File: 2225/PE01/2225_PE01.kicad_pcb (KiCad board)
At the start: 2 copper layers, 200 x 60 mm, 95 parts

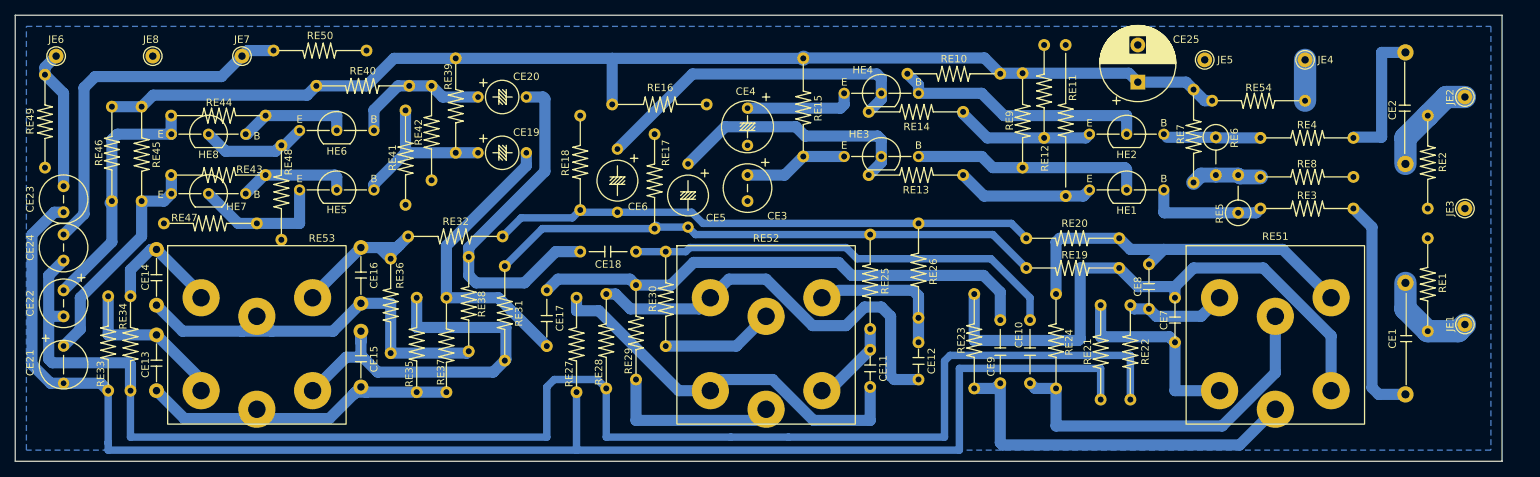
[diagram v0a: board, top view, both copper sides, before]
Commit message: Changed footprints of RE5 and RE6 from vertical resistors to horizontal
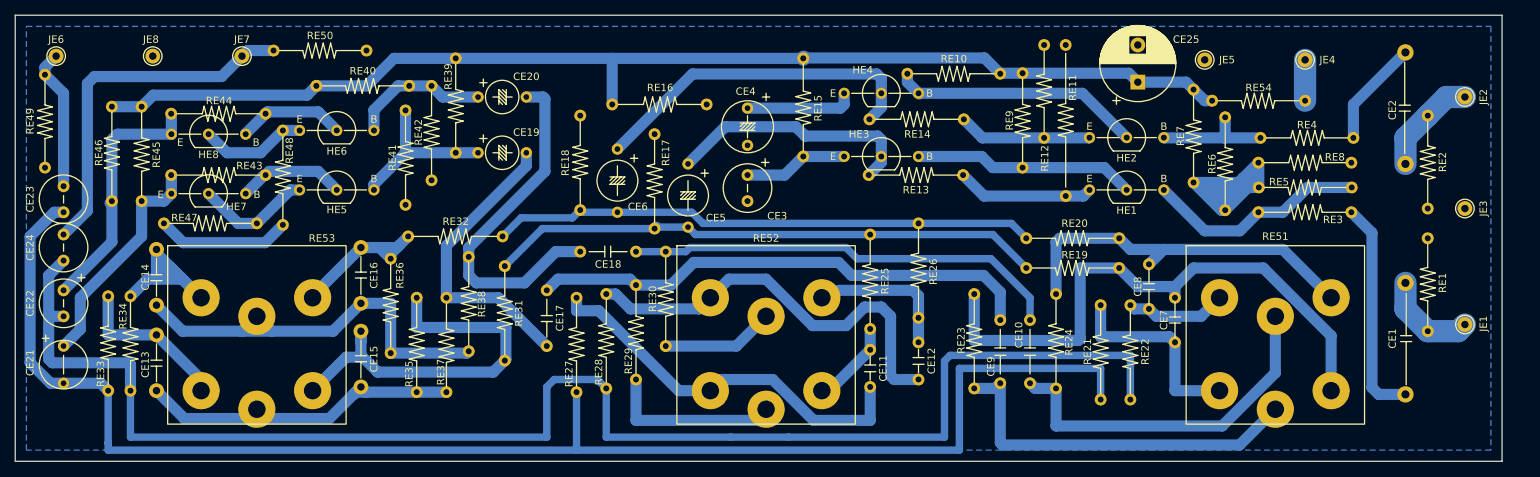
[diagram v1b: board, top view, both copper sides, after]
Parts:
- RE5, RE6: footprint Resistor_THT:R_Axial_DIN0309_L9.0mm_D3.2mm_P5.08mm_Vertical_Flipped -> Resistor_THT:R_US_Axial_DIN0309_L9.0mm_D3.2mm_P12.50mm_Horizontal
- moved RE6 4.89 mm to (162.8, 26.2)
- moved RE5 3.24 mm to (167.3, 23.2), turned to 0 degrees
- moved RE48 2.01 mm to (36.0, 15.5)
- moved RE8 1.94 mm to (179.7, 19.8)
- moved RE14 1.00 mm to (127.6, 14.0)
- moved RE3 0.57 mm to (179.7, 26.5)
- moved HE2 0.46 mm to (144.5, 16.5)
- moved RE44 0.25 mm to (33.7, 13.2)
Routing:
- net Net-(RE5-Pad1): track 9.52 -> 45.4 mm
- net Net-(CE25-Pad2): track 0.00 -> 18.1 mm
- net Net-(RE53-Pad6): track 17.2 -> 31.6 mm
- net Net-(HE1-Pad3): track 16.3 -> 30.0 mm
- net Net-(CE2-Pad2): track 18.5 -> 14.4 mm
- net Net-(HE5-Pad1): track 18.4 -> 15.8 mm
- net Net-(HE2-Pad3): track 13.2 -> 15.8 mm
- net Net-(HE1-Pad2): track 31.5 -> 29.9 mm
- net Net-(HE2-Pad2): track 35.0 -> 33.9 mm
- net Net-(CE6-Pad1): track 45.1 -> 46.1 mm
- net Net-(HE2-Pad1): track 18.8 -> 18.0 mm
- net Net-(HE6-Pad2): track 15.3 -> 14.6 mm
- net Net-(HE5-Pad2): track 15.1 -> 14.5 mm

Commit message: Changed transistor footprints to common packaging spec. Also fixed some trace intersections.
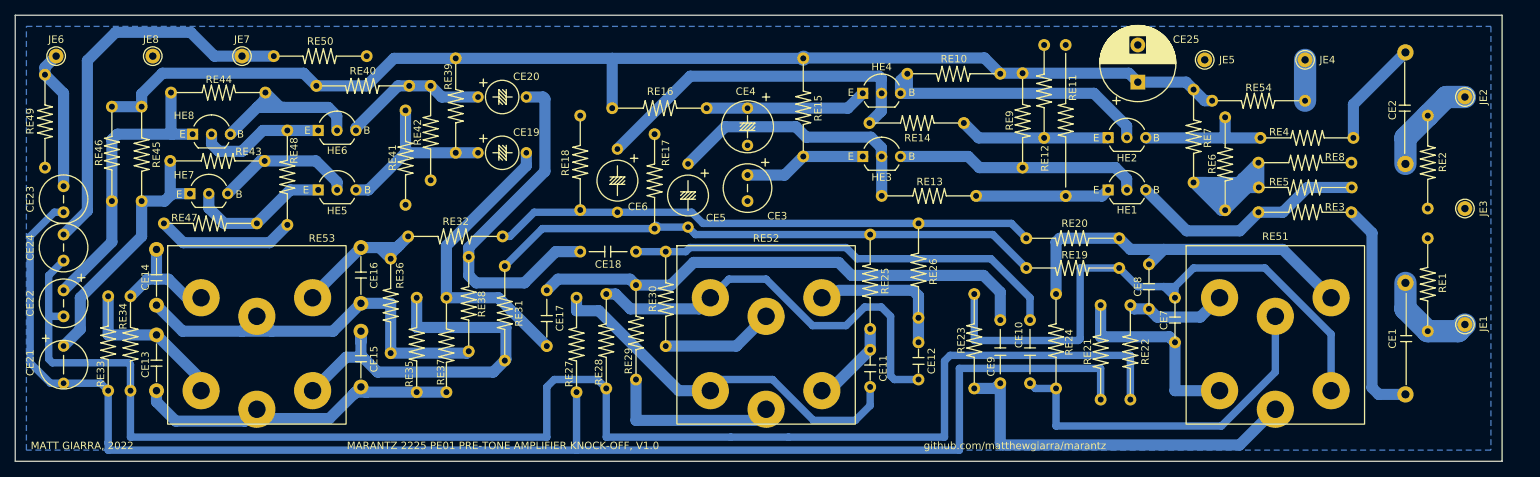
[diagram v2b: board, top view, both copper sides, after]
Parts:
- HE1, HE2, HE3, HE4, HE5, HE6, HE7, HE8: footprint Package_TO_SOT_THT:TO-92_Inline_Wide_10mm -> Package_TO_SOT_THT:TO-92_Inline_Wide
- moved RE13 3.30 mm to (129.2, 24.3)
- moved HE8 2.86 mm to (23.9, 16.0)
- moved RE44 2.85 mm to (33.6, 10.4)
- moved HE1 2.50 mm to (147.0, 23.5)
- moved HE2 2.50 mm to (147.0, 16.5)
- moved HE3 2.50 mm to (114.0, 19.0)
- moved HE4 2.50 mm to (114.0, 10.5)
- moved HE5 2.50 mm to (40.8, 23.5)
- moved HE6 2.50 mm to (40.8, 15.5)
- moved HE7 2.50 mm to (23.5, 24.0)
- moved RE43 1.90 mm to (33.5, 19.6)
- moved RE50 0.75 mm to (34.8, 5.50)
- moved RE48 0.60 mm to (36.6, 15.5)
- moved RE14 0.50 mm to (127.6, 14.5)
- moved RE16 0.50 mm to (93.0, 12.5)
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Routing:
- net Net-(RE53-Pad6): track 31.6 -> 16.5 mm
- net Net-(HE6-Pad2): track 14.6 -> 26.1 mm
- net Net-(CE4-Pad1): track 14.7 -> 21.8 mm
- net Net-(HE2-Pad2): track 33.9 -> 39.5 mm
- net Net-(CE22-Pad1): track 34.4 -> 39.8 mm
- net Net-(HE5-Pad2): track 14.5 -> 18.8 mm
- net Net-(CE21-Pad1): track 30.8 -> 35.0 mm
- net Net-(CE24-Pad2): track 48.5 -> 52.7 mm
- net Net-(HE5-Pad1): track 15.8 -> 19.4 mm
- net Net-(HE1-Pad2): track 29.9 -> 33.2 mm
- net Net-(CE25-Pad1): track 159.3 -> 162.2 mm
- net Net-(HE6-Pad1): track 14.5 -> 17.2 mm
- net Net-(CE3-Pad1): track 14.0 -> 16.5 mm
- net Net-(HE1-Pad3): track 30.0 -> 32.4 mm
- net Net-(HE2-Pad3): track 15.8 -> 18.2 mm
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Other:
- board text added: "MARANTZ 2225 PE01 PRE-TONE AMPLIFIER KNOCK-OFF, V1.0"
- board text added: "MATT GIARRA, 2022"
- board text added: "github.com/matthewgiarra/marantz"

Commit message: Changed some capacitor footprints to match real components
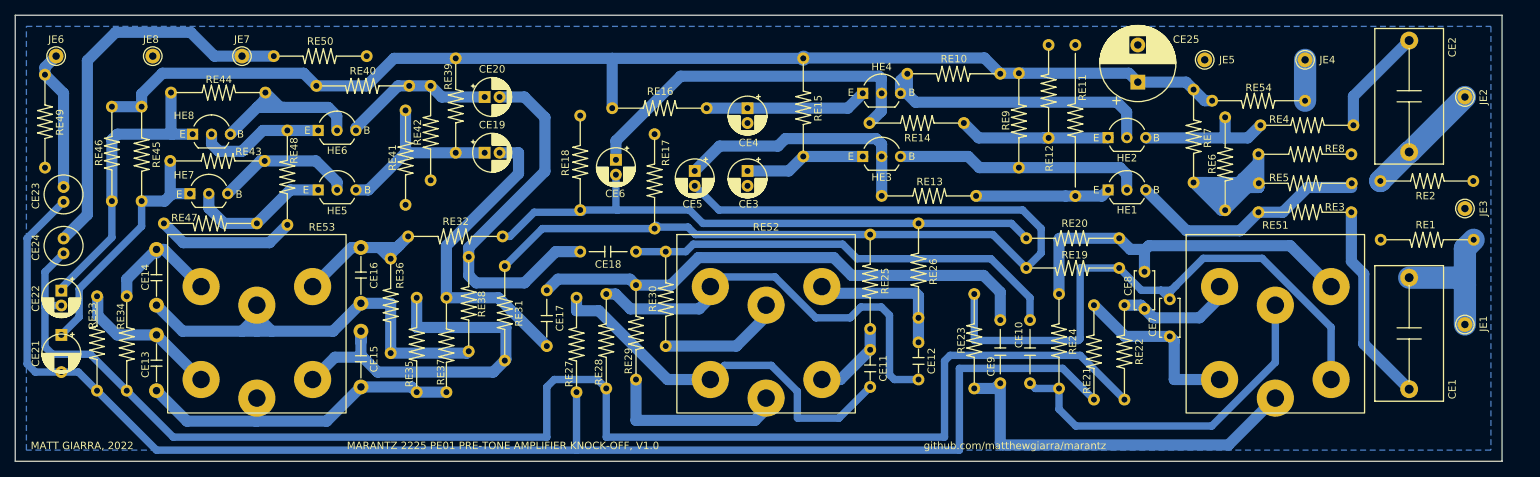
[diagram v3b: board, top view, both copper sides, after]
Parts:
- CE1, CE2: footprint Capacitor_THT:C_US_Rect_L16.5mm_W4.7mm_P15.00mm_MKT -> Capacitor_THT:C_US_Rect_L18.0mm_W9.0mm_P15.00mm_FKS3_FKP3
- CE19, CE20: footprint Capacitor_THT:CP_Electrolytic_Radial_D4.5mm_P6.50mm -> Capacitor_THT:CP_Radial_D5.0mm_P2.00mm
- CE21: footprint Capacitor_THT:CP_Radial_D6.3mm_P5.0mm -> Capacitor_THT:CP_Radial_D5.0mm_P5.00mm
- CE22, CE3: footprint Capacitor_THT:CP_Radial_D6.3mm_H11.0mm_P3.50mm -> Capacitor_THT:CP_Radial_D5.0mm_P2.00mm
- CE23, CE24: footprint Capacitor_THT:C_Radial_D6.3mm_H11.0mm_P3.50mm -> Capacitor_THT:C_Radial_D5.0mm_H11.0mm_P2.00mm
- CE4: footprint Capacitor_THT:CP_Radial_D7.0mm_P5.00mm -> Capacitor_THT:CP_Radial_D5.0mm_P2.00mm
- CE5, CE6: footprint Capacitor_THT:CP_Electrolytic_Radial_D5.5mm_P8.50mm -> Capacitor_THT:CP_Radial_D5.0mm_P2.00mm
- CE7, CE8: footprint Capacitor_THT:C_US_Disc_D7.0mm_W2.5mm_P6.00mm -> Capacitor_THT:C_Disc_D5.0mm_W2.5mm_P5.00mm
- moved RE2 7.16 mm to (196.1, 22.3), turned to 180 degrees
- moved RE1 6.33 mm to (183.7, 30.2), turned to 0 degrees
- moved RE4 1.70 mm to (180.0, 14.8)
- moved CE2 1.68 mm to (187.5, 18.4)
- moved RE33 1.50 mm to (11.0, 37.8)
- moved RE51 1.50 mm to (162.0, 49.0)
- moved RE52 1.50 mm to (93.5, 49.0)
- moved RE53 1.50 mm to (25.0, 49.0)
- moved CE6 1.46 mm to (80.8, 19.4)
- moved CE23 1.40 mm to (6.50, 25.1)
- moved CE5 1.30 mm to (91.4, 20.9)
- moved RE11 1.30 mm to (142.6, 4.00)
- moved RE8 1.13 mm to (179.7, 18.7)
- moved CE7 1.06 mm to (155.3, 43.2)
- moved CE24 0.97 mm to (6.50, 32.0)
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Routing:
- net Net-(CE5-Pad2): track 74.6 -> 129.7 mm
- net Net-(CE22-Pad2): track 202.4 -> 193.3 mm
- net Net-(CE21-Pad2): track 199.5 -> 192.7 mm
- net Net-(CE1-Pad1): track 13.4 -> 20.1 mm
- net Net-(CE6-Pad2): track 73.6 -> 78.9 mm
- net Net-(RE53-Pad5): track 57.5 -> 62.5 mm
- net Net-(RE51-Pad1): track 27.1 -> 24.1 mm
- net Net-(CE1-Pad2): track 29.6 -> 27.0 mm
- net Net-(RE52-Pad4): track 17.3 -> 19.8 mm
- net Net-(RE51-Pad6): track 13.7 -> 16.1 mm
- net Net-(CE2-Pad1): track 13.8 -> 16.1 mm
- net Net-(CE6-Pad1): track 46.3 -> 48.6 mm
- net Net-(RE5-Pad1): track 45.4 -> 47.6 mm
- net Net-(CE18-Pad2): track 47.8 -> 49.9 mm
- net Net-(CE17-Pad2): track 40.1 -> 42.3 mm
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
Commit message: Updated footprints of CE9 - CE12. Changed some trace widths to 0.5mm
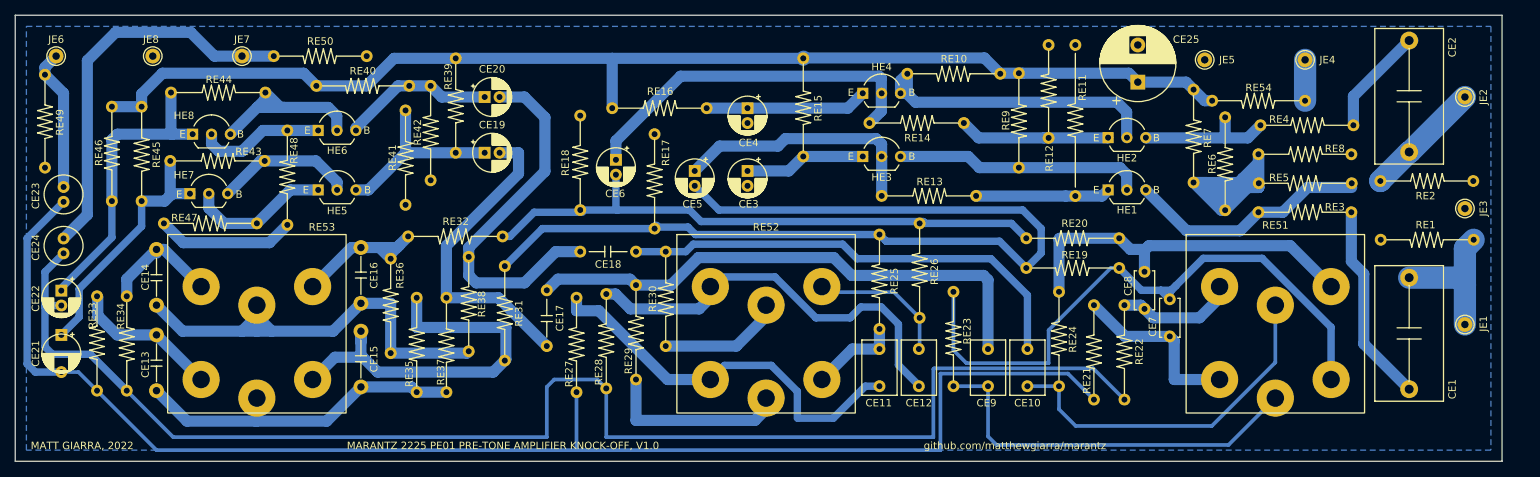
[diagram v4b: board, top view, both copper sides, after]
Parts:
- CE10, CE9: footprint Capacitor_THT:C_Rect_L7.2mm_W3.5mm_P8.50mm -> Capacitor_THT:C_Rect_L7.2mm_W4.5mm_P5.00mm_FKS2_FKP2_MKS2_MKP2
- CE11, CE12: footprint Capacitor_THT:C_US_Rect_L7.2mm_W3.5mm_P5.00mm_FKS2_FKP2_MKS2_MKP2 -> Capacitor_THT:C_Rect_L7.2mm_W4.5mm_P5.00mm_FKS2_FKP2_MKS2_MKP2
- moved RE23 2.82 mm to (126.2, 37.2)
- moved CE9 1.70 mm to (130.8, 49.9)
- moved CE11 1.25 mm to (116.2, 49.9)
- moved RE25 1.25 mm to (116.2, 29.5)
- moved CE12 0.90 mm to (121.5, 49.9)
- moved CE10 0.53 mm to (136.2, 49.9)
- moved RE24 0.30 mm to (140.4, 37.2)
- moved RE26 0.15 mm to (121.7, 28.0)
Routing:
- net Net-(CE10-Pad2): track 59.4 -> 62.9 mm
- net Net-(RE51-Pad3): track 81.6 -> 85.1 mm
- net Net-(CE17-Pad1): track 69.2 -> 72.2 mm
- net Net-(CE22-Pad2): track 193.3 -> 191.2 mm
- net Net-(RE51-Pad2): track 51.6 -> 53.5 mm
- net Net-(RE52-Pad1): track 52.6 -> 53.8 mm
- net Net-(RE52-Pad3): track 11.0 -> 12.1 mm
- net Net-(CE21-Pad2): track 192.7 -> 191.7 mm
- net Net-(RE52-Pad6): track 55.6 -> 54.7 mm
- net Net-(RE52-Pad4): track 19.8 -> 20.4 mm

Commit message: Changed footprint of CE13 and CE14 to real WIMA caps.
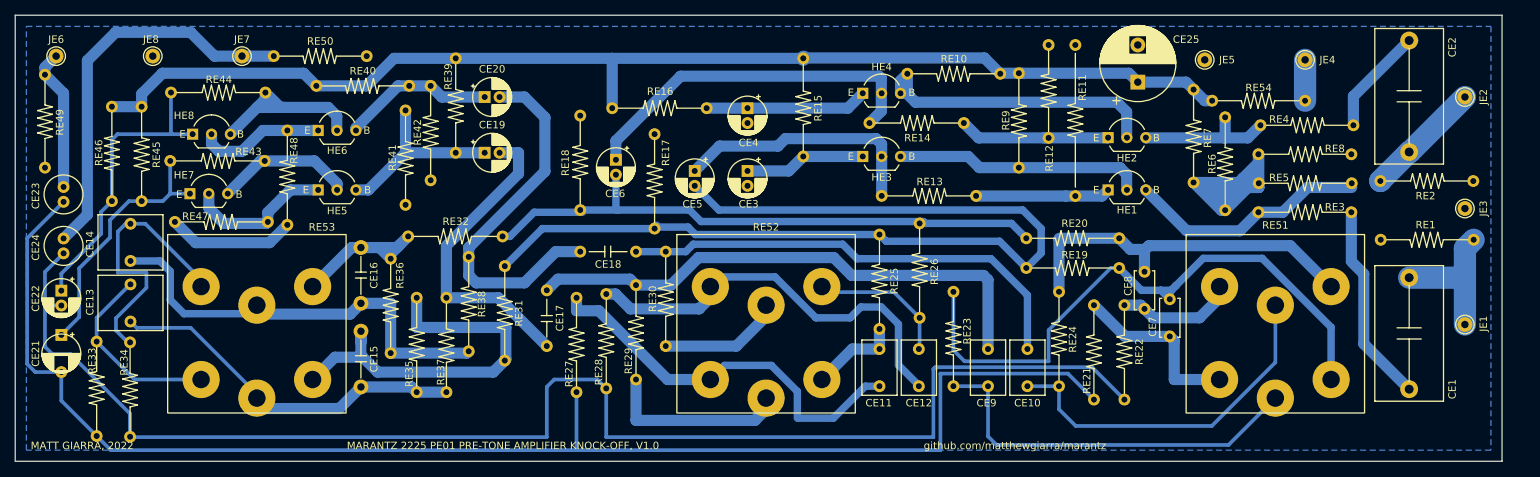
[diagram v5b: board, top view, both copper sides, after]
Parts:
- CE13, CE14: footprint Capacitor_THT:C_US_Rect_L10.0mm_W4.0mm_P7.50mm_FKS3_FKP3 -> Capacitor_THT:C_Rect_L7.2mm_W8.5mm_P5.00mm_FKP2_FKP2_MKS2_MKP2
- moved CE13 7.65 mm to (15.5, 36.2)
- moved RE34 6.22 mm to (15.4, 56.7)
- moved RE33 6.10 mm to (10.9, 43.9)
- moved CE14 4.91 mm to (15.5, 28.1)
- moved RE47 1.49 mm to (21.5, 27.8)
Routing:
- net Net-(RE53-Pad6): track 17.0 -> 37.7 mm
- net Net-(CE22-Pad2): track 191.2 -> 196.7 mm
- net Net-(RE53-Pad1): track 21.6 -> 26.7 mm
- net Net-(RE53-Pad2): track 46.0 -> 49.4 mm
- net Net-(CE21-Pad2): track 191.7 -> 194.1 mm
- net Net-(RE53-Pad5): track 62.5 -> 60.7 mm
- net Net-(CE25-Pad2): track 18.7 -> 17.3 mm
- net Net-(CE21-Pad1): track 33.6 -> 34.4 mm
- net Net-(HE5-Pad1): track 19.4 -> 20.1 mm

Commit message: Updated capacitor footprints to represent available components
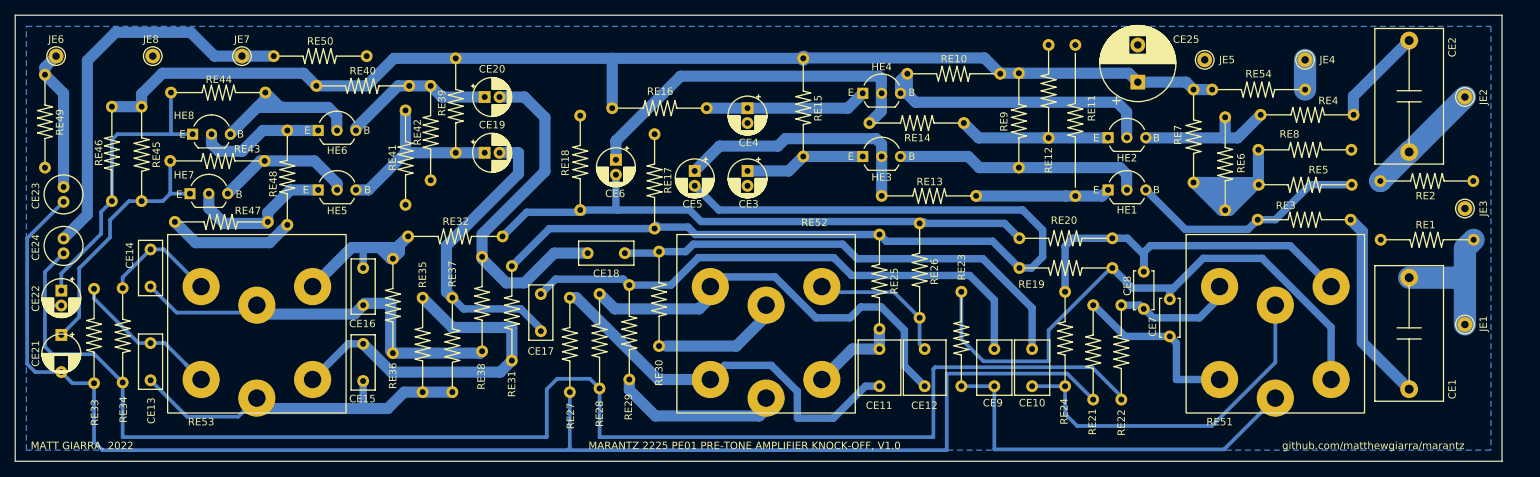
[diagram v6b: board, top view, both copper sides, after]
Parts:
- CE11, CE12: footprint Capacitor_THT:C_Rect_L7.2mm_W4.5mm_P5.00mm_FKS2_FKP2_MKS2_MKP2 -> Capacitor_THT:C_Rect_L7.2mm_W5.5mm_P5.00mm_FKS2_FKP2_MKS2_MKP2
- CE13, CE14: footprint Capacitor_THT:C_Rect_L7.2mm_W8.5mm_P5.00mm_FKP2_FKP2_MKS2_MKP2 -> Capacitor_THT:C_Rect_L7.2mm_W3.0mm_P5.00mm_FKS2_FKP2_MKS2_MKP2
- CE15, CE16: footprint Capacitor_THT:C_US_Rect_L10.0mm_W4.0mm_P7.50mm_FKS3_FKP3 -> Capacitor_THT:C_Rect_L7.2mm_W3.0mm_P5.00mm_FKS2_FKP2_MKS2_MKP2
- CE17, CE18: footprint Capacitor_THT:C_US_Rect_L9.0mm_W3.2mm_P7.50mm_MKT -> Capacitor_THT:C_Rect_L7.2mm_W3.0mm_P5.00mm_FKS2_FKP2_MKS2_MKP2
- moved CE13 8.35 mm to (18.2, 44.1)
- moved RE34 7.37 mm to (14.4, 49.4)
- moved RE33 7.11 mm to (10.6, 36.8)
- moved CE14 4.38 mm to (18.2, 31.5)
- moved RE38 1.80 mm to (62.8, 32.5)
- moved CE18 1.51 mm to (82.0, 32.0)
- moved RE54 1.50 mm to (161.0, 10.0)
- moved RE4 1.40 mm to (180.0, 13.4)
- moved RE23 1.07 mm to (127.3, 37.2)
- moved RE3 1.00 mm to (179.6, 27.5)
- moved RE31 0.95 mm to (66.8, 33.8)
- moved CE17 0.94 mm to (70.7, 37.5)
- moved RE19 0.93 mm to (135.1, 34.0)
- moved RE20 0.93 mm to (135.1, 30.0)
- moved RE27 0.90 mm to (74.6, 38.0)
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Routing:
- net Net-(RE53-Pad6): track 37.7 -> 17.1 mm
- net Net-(RE5-Pad1): track 47.6 -> 38.0 mm
- net Net-(RE53-Pad5): track 60.7 -> 54.6 mm
- net Net-(RE51-Pad3): track 84.7 -> 80.1 mm
- net Net-(RE53-Pad3): track 54.2 -> 50.5 mm
- net Net-(RE53-Pad4): track 20.3 -> 23.5 mm
- net Net-(CE18-Pad2): track 49.9 -> 46.9 mm
- net Net-(CE21-Pad2): track 194.1 -> 196.4 mm
- net Net-(RE53-Pad1): track 26.7 -> 24.7 mm
- net Net-(RE52-Pad2): track 23.6 -> 21.6 mm
- net Net-(CE17-Pad2): track 42.3 -> 40.3 mm
- net Net-(JE4-Pad1): track 5.50 -> 4.00 mm
- net Net-(CE2-Pad2): track 15.1 -> 13.7 mm
- net Net-(CE22-Pad2): track 196.7 -> 195.5 mm
- net Net-(RE52-Pad6): track 54.7 -> 55.8 mm
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
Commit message: Cleaned up traces and made most of them 1mm
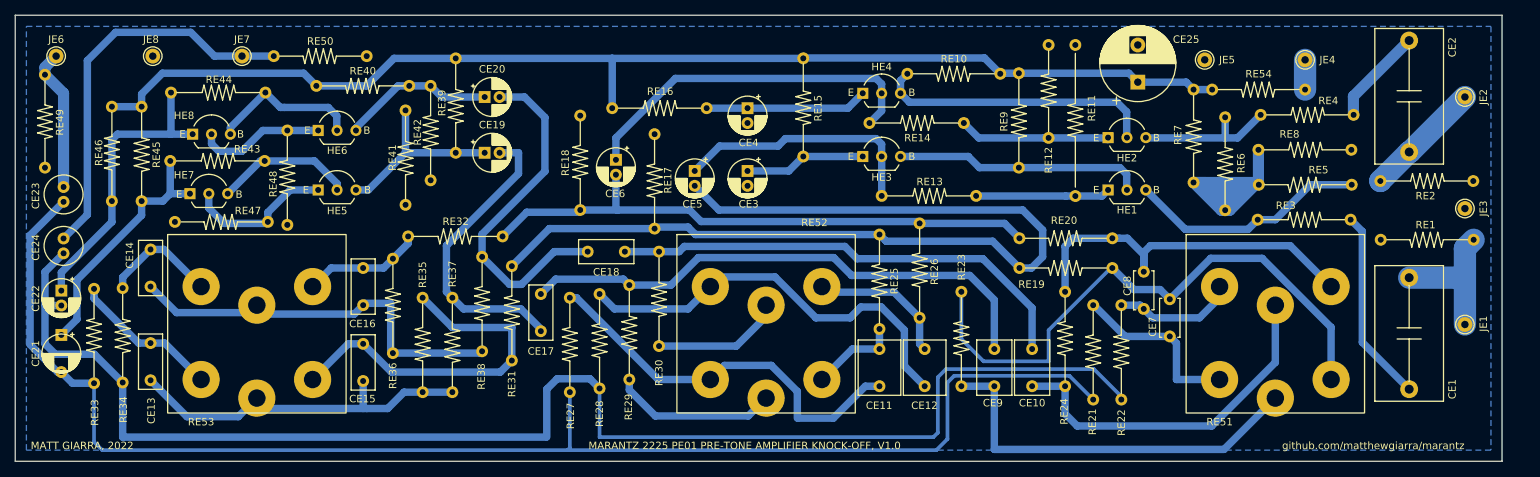
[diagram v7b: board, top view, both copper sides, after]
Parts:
- moved CE18 0.20 mm to (82.0, 31.8)
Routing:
- net Net-(CE25-Pad2): track 17.3 -> 0.00 mm
- net Net-(RE53-Pad4): track 23.5 -> 16.2 mm
- net Net-(HE6-Pad2): track 26.1 -> 20.4 mm
- net Net-(RE53-Pad1): track 24.7 -> 20.2 mm
- net Net-(CE21-Pad2): track 196.4 -> 192.5 mm
- net Net-(HE2-Pad2): track 40.6 -> 37.9 mm
- net Net-(CE22-Pad2): track 195.5 -> 194.0 mm
- net Net-(RE53-Pad6): track 17.1 -> 15.6 mm
- net Net-(RE53-Pad3): track 50.5 -> 49.1 mm
- net Net-(RE52-Pad4): track 20.6 -> 19.4 mm
- net Net-(RE52-Pad5): track 16.7 -> 17.6 mm
- net Net-(RE53-Pad2): track 49.6 -> 48.9 mm
- net Net-(RE52-Pad6): track 55.8 -> 56.5 mm
- net Net-(RE52-Pad2): track 21.6 -> 22.2 mm
- net Net-(CE2-Pad2): track 13.7 -> 13.1 mm
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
